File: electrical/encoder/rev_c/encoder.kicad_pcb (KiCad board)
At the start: 2 copper layers, 14.8 x 48 mm, 5 parts, among them CN1 ENCODER;2xM1x3RA, Q1 AH1806;SC59, Q2 AH1806;SC59

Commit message: Wrapped up Encoder Rev. C.
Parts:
- Q1, Q2: value AH1806;SC59 -> DRV5013FAQDBZR;SOT23; footprint HR2:SC59 -> Package_TO_SOT_SMD:SOT-23
- R1, R2: value 100Ω;1005 -> 47KΩ;1608; footprint Resistor_SMD:R_0402_1005Metric -> Resistor_SMD:R_0603_1608Metric
- moved Q1 0.33 mm to (96.8, 96.8), turned to 225 degrees
- moved Q2 0.33 mm to (96.8, 103.2), turned to 135 degrees
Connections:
- Q1 pad 2: /GND -> /QUADB
- Q1 pad 3: /QUADB -> /GND
- Q2 pad 2: /GND -> /QUADA
- Q2 pad 3: /QUADA -> /GND
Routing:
- net /QUADA: track 24.2 -> 23.5 mm
- net /GND: track 38.9 -> 39.5 mm

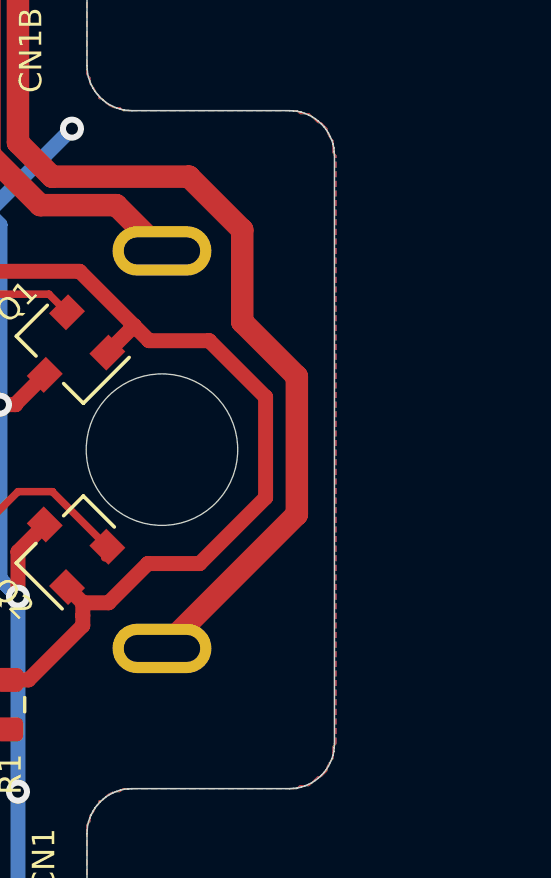
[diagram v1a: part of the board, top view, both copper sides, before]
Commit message: Added more testing programs and made edits to rev_c enocder
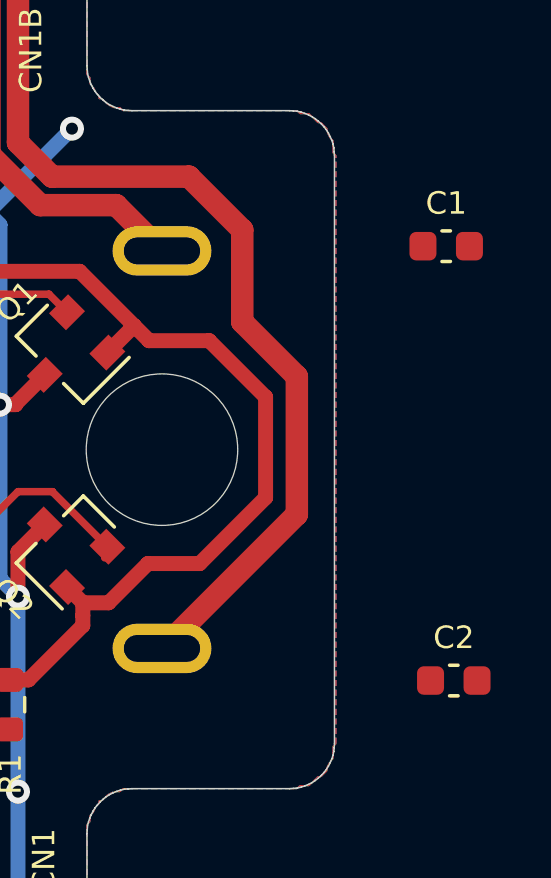
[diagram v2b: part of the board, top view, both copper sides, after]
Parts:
- added C1: 10nF;1608, Capacitor_SMD:C_0603_1608Metric, F.Cu at (109.5, 93.2)
- added C2: 10nF;1608, Capacitor_SMD:C_0603_1608Metric, F.Cu at (109.7, 107.7)
- R1, R2: value 47KΩ;1608 -> 10KΩ;1608

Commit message: Created electrical/encoder/rev_c gerber/drill/zip files.
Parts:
- moved C1 17.1 mm to (93.0, 88.5), turned to 90 degrees
- moved C2 12.2 mm to (97.7, 109.3)
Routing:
- net /GND: track 39.5 -> 50.3 mm, vias 5 -> 6
- net /VCC: track 40.0 -> 43.2 mm
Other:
- board text added: "HR2 Encoder Rev C: 2021APR02"
- board text removed: "HR2 Encoder Rev C: 2021MAR03"
